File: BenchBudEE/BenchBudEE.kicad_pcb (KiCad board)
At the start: 4 copper layers, 165.1 x 63.5 mm, 0 parts

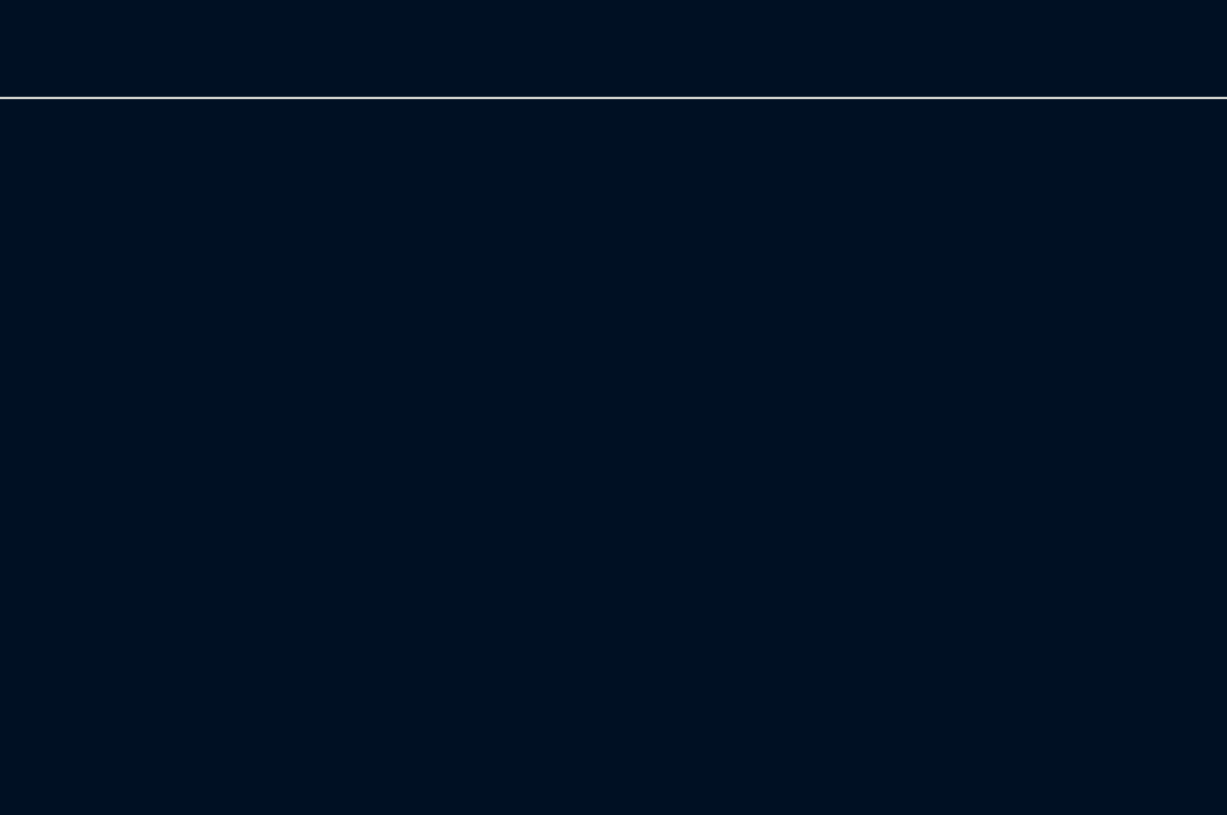
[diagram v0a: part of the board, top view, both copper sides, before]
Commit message: Placed the relay components.
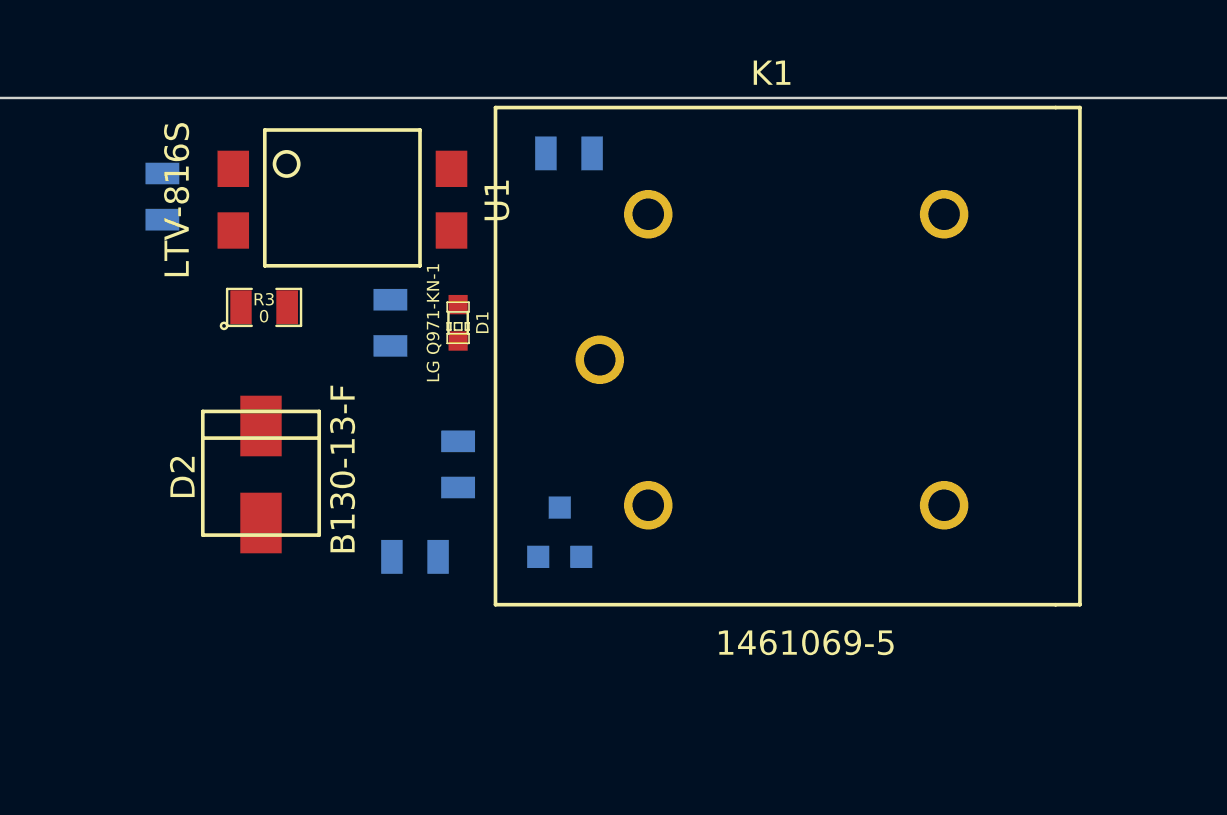
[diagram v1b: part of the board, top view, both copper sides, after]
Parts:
- added D1: LG Q971-KN-1, LED-0603, F.Cu at (209.0, 122.3)
- added D2: B130-13-F, SMA, F.Cu at (200.9, 130.6)
- added K1: 1461069-5, TE-SPDT, F.Cu at (214.9, 123.8)
- added Q1: 2N3904, SOT23EBC, B.Cu at (213.2, 130.9)
- added R1: 500, SM0805, B.Cu at (196.8, 117.1)
- added R2: 200, SM0805, B.Cu at (206.2, 122.3)
- added R3: 0, SM0805, F.Cu at (201.0, 121.7)
- added R4: 100, SM0805, B.Cu at (209.0, 128.1)
- added R5: 0, SM0805, B.Cu at (213.6, 115.3)
- added R6: 0, SM0805, B.Cu at (207.3, 132.0)
- added U1: LTV-816S, 4-SMD, F.Cu at (199.8, 116.0)

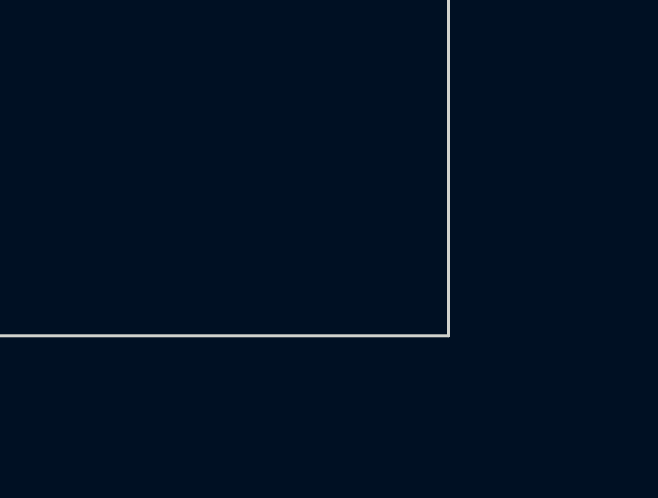
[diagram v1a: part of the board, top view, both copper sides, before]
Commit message: Associated the Thermocouple components.
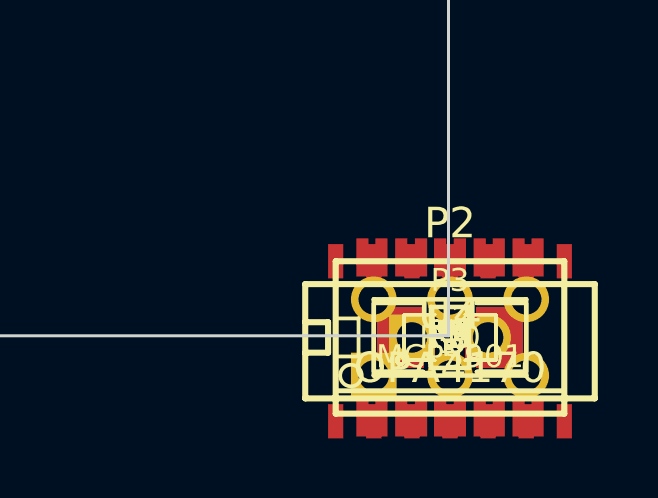
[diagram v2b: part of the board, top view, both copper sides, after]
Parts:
- added C1, C10, C11, C7, C8, C9: C, SM0805, F.Cu at (247.2, 176.6)
- added P2: CONN_3X2, pin_array_3x2, F.Cu at (247.2, 176.6)
- added P3: CONN_2, PIN_ARRAY_2X1, F.Cu at (247.2, 176.6)
- added R10, R7, R8, R9: R, SM1206, F.Cu at (247.2, 176.6)
- added R11, R12, R13, R44, R45: R, SM0805, F.Cu at (247.2, 176.6)
- added U2: MCP3901, SSOP20, F.Cu at (247.2, 176.6)
- added U3: LMT84, SOT353, F.Cu at (247.2, 176.6)
- added U4: OPA4170, SO14E, F.Cu at (247.2, 176.6)

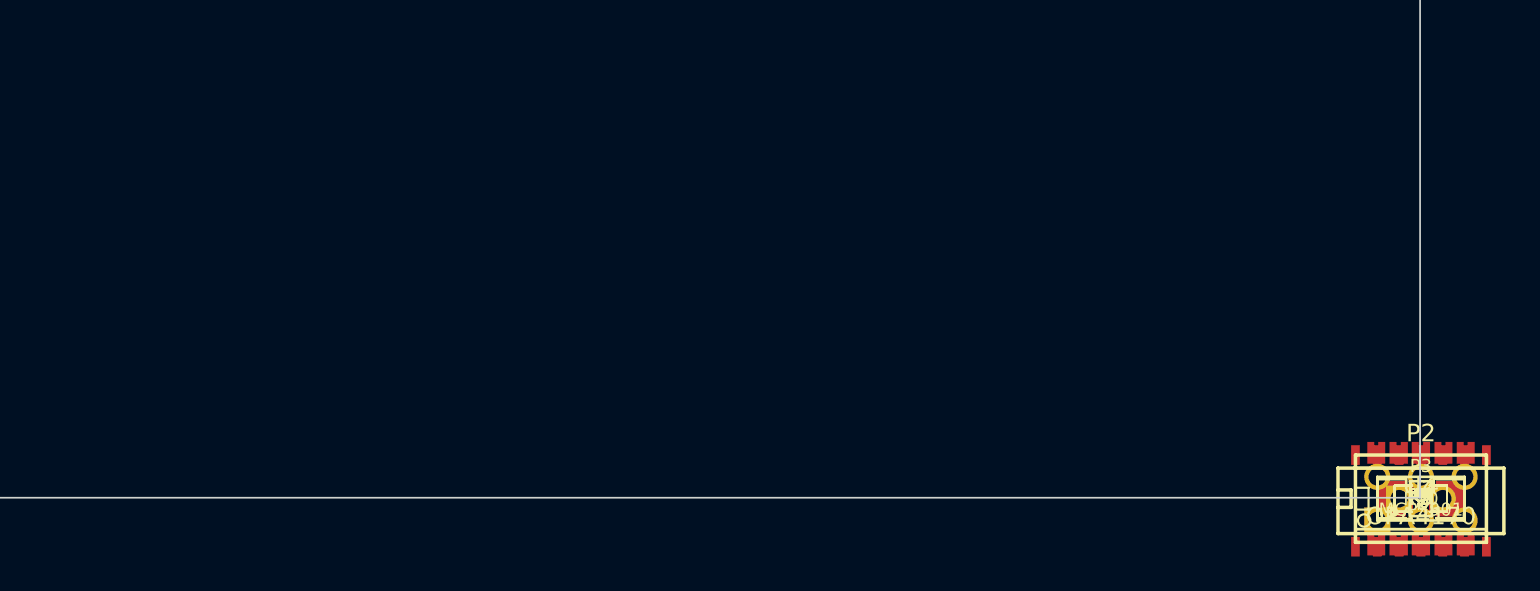
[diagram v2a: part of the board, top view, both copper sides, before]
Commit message: Roughly placed the Thermocouple components.
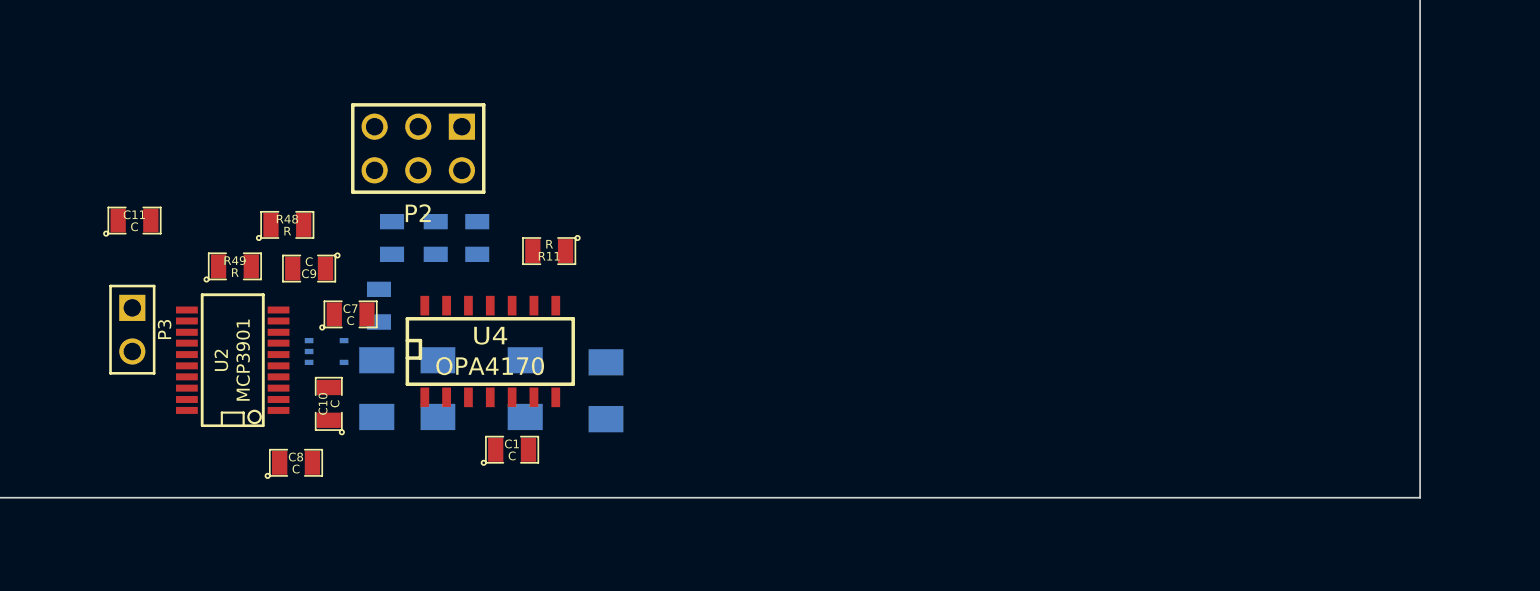
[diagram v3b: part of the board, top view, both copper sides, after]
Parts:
- added R48: R, SM0805, F.Cu at (181.2, 160.7)
- added R49: R, SM0805, F.Cu at (178.2, 163.1)
- R10, R12, R13, R44, R45, R7, R8, R9, U3: moved to B.Cu
- moved C11 76.6 mm to (172.3, 160.4)
- moved P3 75.6 mm to (172.2, 166.8), turned to 270 degrees
- moved U2 69.6 mm to (178.1, 168.5), turned to 90 degrees
- moved C9 66.1 mm to (182.5, 163.2), turned to 180 degrees
- moved C8 65.5 mm to (181.7, 174.5)
- moved U3 64.3 mm to (183.5, 168.0)
- moved C10 63.8 mm to (183.6, 171.1), turned to 90 degrees
- moved C7 63.2 mm to (184.9, 165.9)
- moved P2 61.8 mm to (188.8, 156.2), turned to 180 degrees
- moved R12 61.8 mm to (187.3, 161.4), turned to 270 degrees
- moved R13 61.7 mm to (186.6, 165.4), turned to 270 degrees
- moved R8 61.1 mm to (186.4, 170.2), turned to 270 degrees
- moved R45 59.3 mm to (189.9, 161.4), turned to 270 degrees
- moved R10 57.6 mm to (190.0, 170.2), turned to 270 degrees
- moved R44 57.0 mm to (192.3, 161.4), turned to 270 degrees
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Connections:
- R7 pad 1: N-0000070 (its old number) -> /Thermocouple/CH0+
- U2 pad 4: N-0000070 (its old number) -> /Thermocouple/CH0+
- U2 pad 5: +5V -> /Thermocouple/CH0-
- U2 pad 6: +5V -> /Thermocouple/CH1-
- U2 pad 7: N-0000058 (its old number) -> /Thermocouple/CH1+
- U3 pad 3: N-0000058 (its old number) -> /Thermocouple/CH1+
- U4 pad 1: N-0000070 (its old number) -> /Thermocouple/CH0+

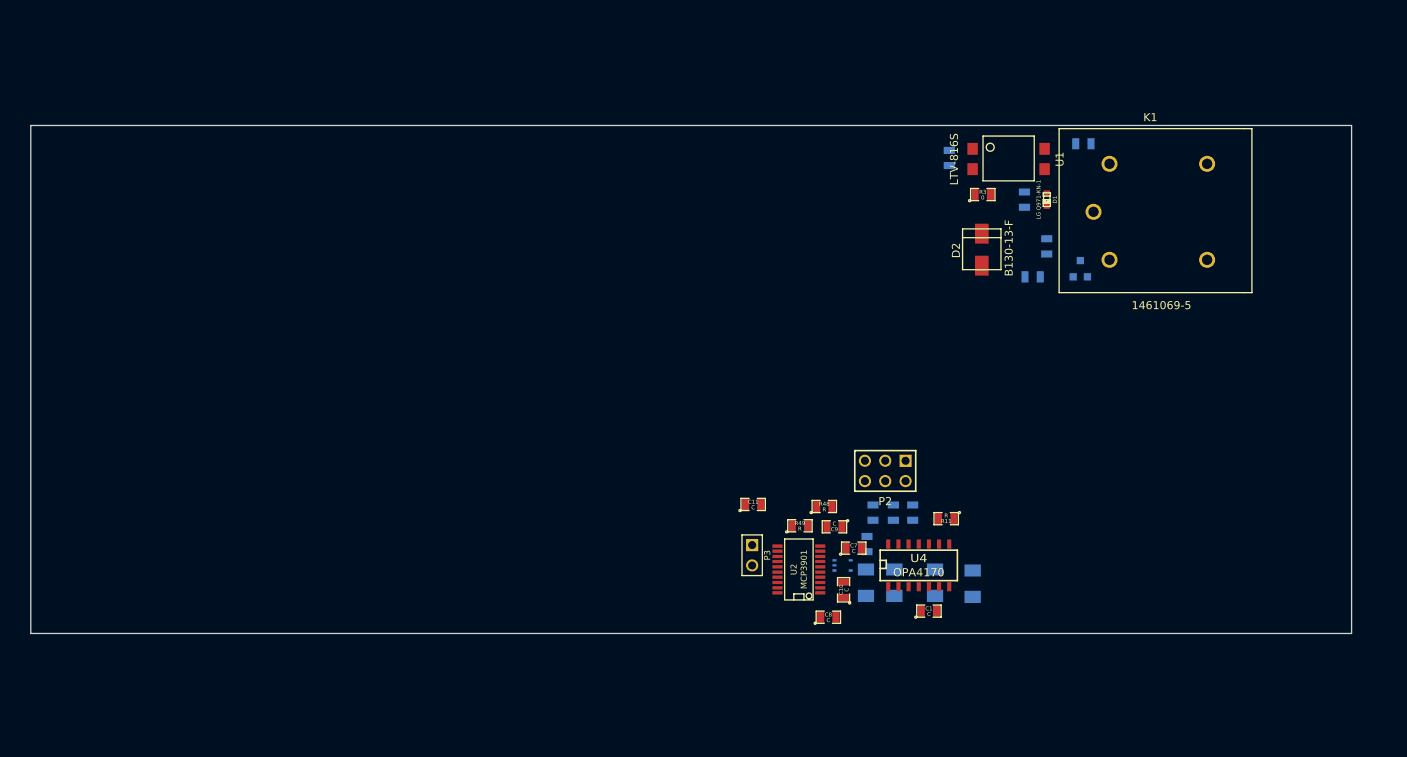
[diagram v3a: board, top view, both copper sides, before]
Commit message: Placed the Terminal/ATX block components.
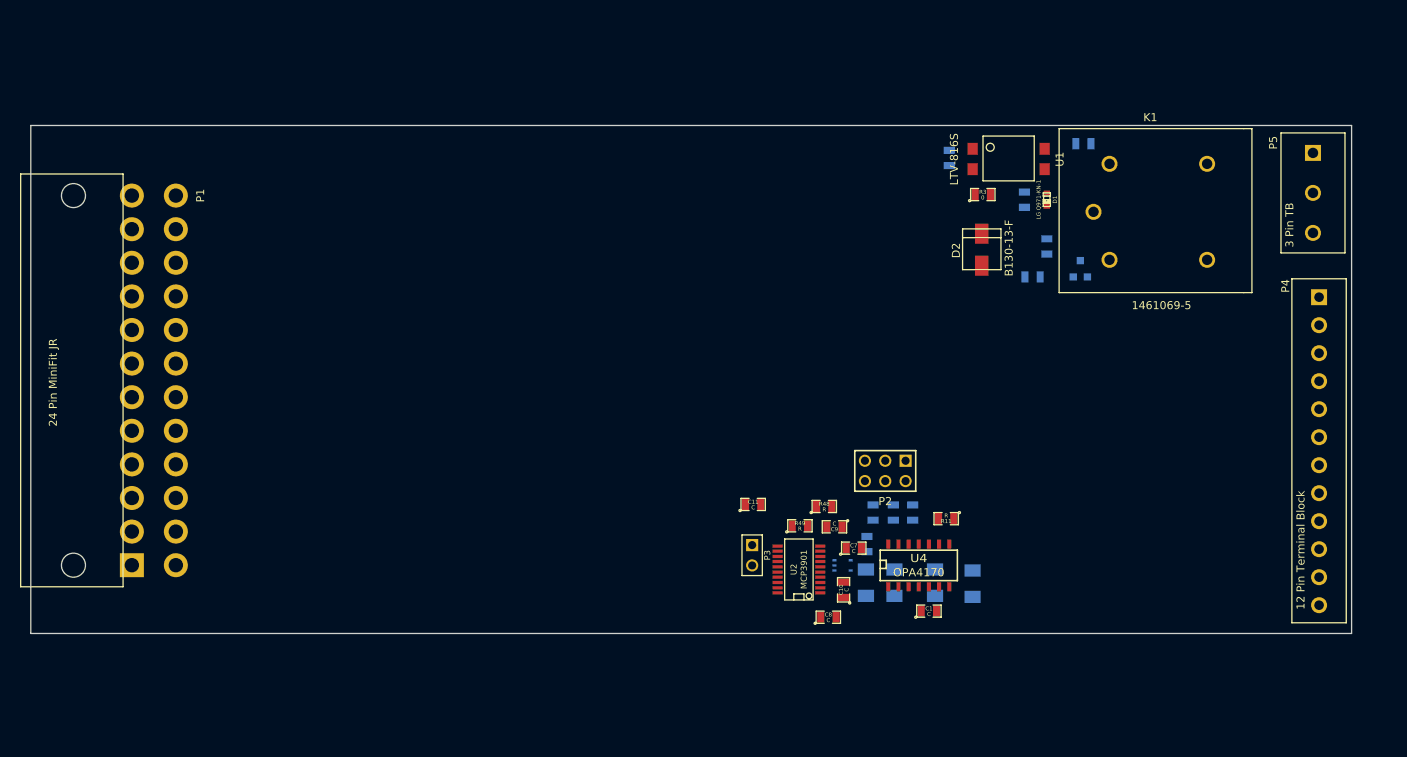
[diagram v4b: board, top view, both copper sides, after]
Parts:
- added P1: 24 Pin MiniFit JR, ATX_Header, F.Cu at (87.4, 121.8)
- added P4: 12 Pin Terminal Block, 12PinTB, F.Cu at (243.1, 134.5)
- added P5: 3 Pin TB, 3PinTB, F.Cu at (242.3, 116.5)
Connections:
- K1 pad 1: (no net) -> /Relay/RELAY_COM
- K1 pad 3: (no net) -> /Relay/RELAY_NO
- K1 pad 4: (no net) -> /Relay/RELAY_NC
- U4 pad 10: (no net) -> /Thermocouple/TC IN +
- U4 pad 12: (no net) -> /Thermocouple/TC IN -

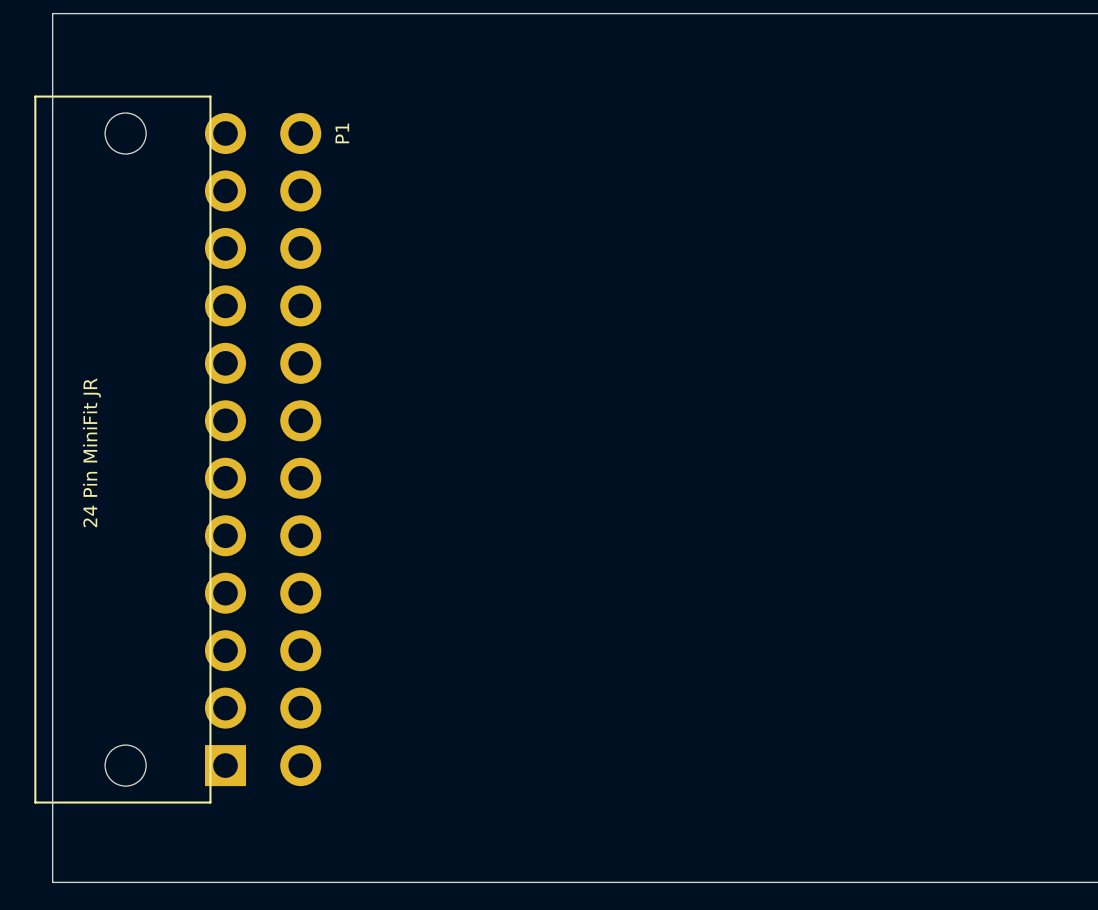
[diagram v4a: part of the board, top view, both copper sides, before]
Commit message: Associated and placed the Arduino module.
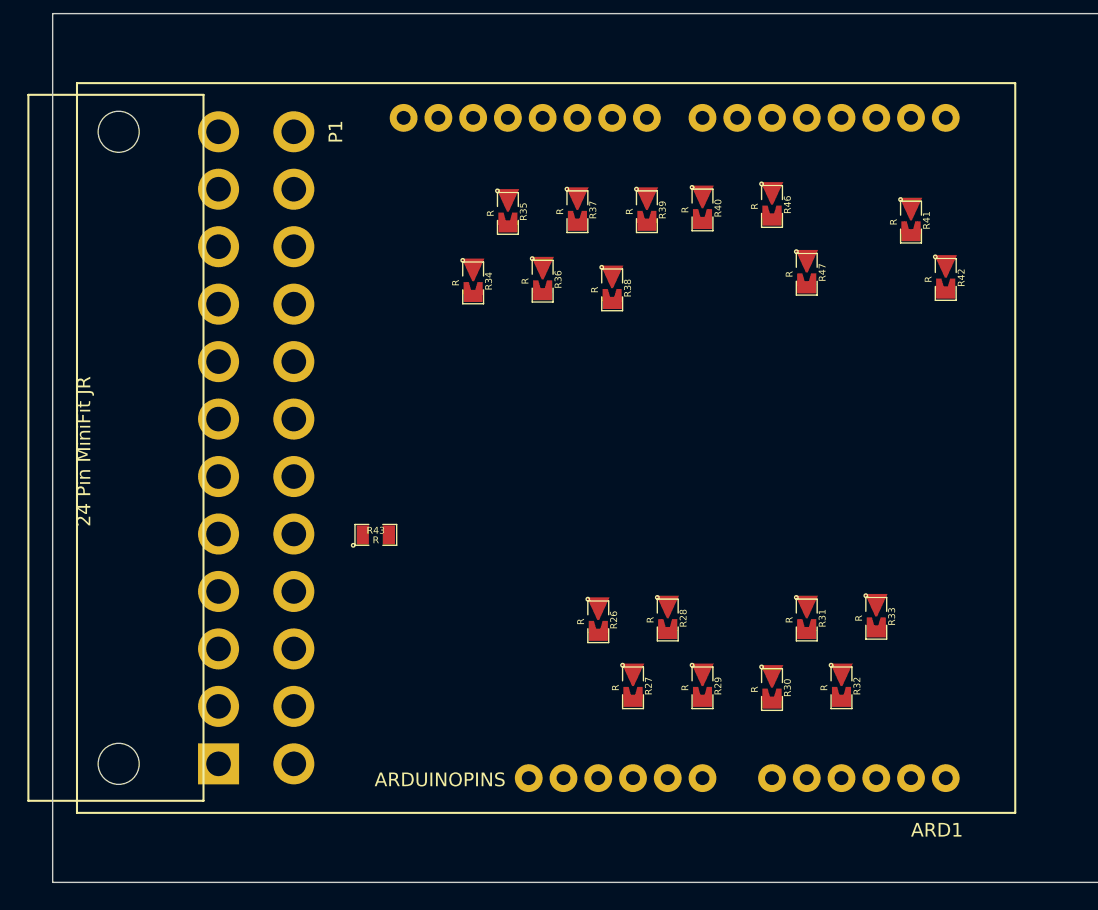
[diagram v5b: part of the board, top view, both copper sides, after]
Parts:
- added ARD1: ARDUINOPINS, Arduino, F.Cu at (118.1, 144.8)
- added R26: R, SM0805-blob, F.Cu at (121.9, 157.5)
- added R27: R, SM0805-blob, F.Cu at (124.5, 162.3)
- added R28: R, SM0805-blob, F.Cu at (127.0, 157.4)
- added R29: R, SM0805-blob, F.Cu at (129.5, 162.3)
- added R30: R, SM0805-blob, F.Cu at (134.6, 162.4)
- added R31: R, SM0805-blob, F.Cu at (137.2, 157.4)
- added R32: R, SM0805-blob, F.Cu at (139.7, 162.3)
- added R33: R, SM0805-blob, F.Cu at (142.2, 157.2)
- added R34: R, SM0805-blob, F.Cu at (112.8, 132.7)
- added R35: R, SM0805-blob, F.Cu at (115.3, 127.6)
- added R36: R, SM0805-blob, F.Cu at (117.9, 132.6)
- added R37: R, SM0805-blob, F.Cu at (120.4, 127.5)
- added R38: R, SM0805-blob, F.Cu at (122.9, 133.2)
- added R39: R, SM0805-blob, F.Cu at (125.5, 127.5)
- added R40: R, SM0805-blob, F.Cu at (129.5, 127.4)
- added R41: R, SM0805-blob, F.Cu at (144.8, 128.3)
- added R42: R, SM0805-blob, F.Cu at (147.3, 132.5)
- added R43: R, SM0805, F.Cu at (105.7, 151.1)
- added R46: R, SM0805-blob, F.Cu at (134.6, 127.1)
- added R47: R, SM0805-blob, F.Cu at (137.2, 132.1)
- moved P1 0.52 mm to (86.9, 121.7)
